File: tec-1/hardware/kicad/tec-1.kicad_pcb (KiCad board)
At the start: 2 copper layers, 160 x 160 mm, 150 parts, among them J1 USB_C_Receptacle_USB2.0, J2 Conn_01x02, J3 LCD, Q1 2N3904, Q10 AO3400A, Q11 AO3400A, Q12 AO3400A, Q13 AO3400A, Q14 AO3400A, Q15 AO3400A, Q16 AO3400A, Q17 AO3400A, Q18 AO3400A, Q19 AO3400A, Q2 AO3400A, Q20 AO3400A, Q21 AO3400A, Q22 AO3400A, Q23 AO3400A, Q3 AO3400A, Q4 AO3400A, Q5 AO3400A, Q6 AO3400A, Q7 AO3400A, Q8 AO3400A, Q9 AO3400A, SW1 SW_DIP_x04, SW10 SW_0, SW11 SW_7, SW12 SW_6, SW13 SW_5, SW14 SW_4, SW15 SW_B, SW16 SW_A, SW17 SW_9, SW18 SW_8, SW19 SW_F, SW2 SW_SPST, SW20 SW_E, SW21 SW_D, SW22 SW_C, SW3 SW_AD, SW4 SW_GO, SW5 SW_MINUS, SW6 SW_PLUS, SW7 SW_3, SW8 SW_2, SW9 SW_1, U1 IO, U10 74HCT574, U11 74HCT574, U12 LED_SEGMENT_CC_x2, U13 LED_SEGMENT_CC_x4, U14 74HCT574, U15 74HCT574, U16 74HCT574, U2 MEMORY, U3 Z80CPU, U5 SRM2264, U6 SRM2264, U7 FT232RL, U8 MM74C923, U9 KEYDB

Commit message: tec-1/hardware/kicad: progress checkin - add clock & 207 unrouted
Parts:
- added C20: 0.1uF/10V, tec-1:C_0805_2012Metric, F.Cu at (76.3, 82.8)
- added C21: 0.1uF/10V, tec-1:C_0805_2012Metric, B.Cu at (76.5, 99.5)
- added C8: 100uF/10V, tec-1:CP_EIA-7343-31_Kemet-D, F.Cu at (23.0, 147.5)
- added J4: ADDR, tec-1:PinHeader_1x17_P2.54mm_Vertical, F.Cu at (151.5, 68.0)
- added J5: DATA, tec-1:PinHeader_1x09_P2.54mm_Vertical, F.Cu at (160.8, 68.0)
- added R42: 10k, tec-1:R_0805_2012Metric, B.Cu at (79.5, 99.2)
- added R43: DNP, tec-1:R_0805_2012Metric, B.Cu at (84.2, 98.2)
- added R44: 10k, tec-1:R_0805_2012Metric, B.Cu at (52.0, 69.2)
- added R45: 10k, tec-1:R_0805_2012Metric, B.Cu at (52.0, 71.8)
- added R46: 10k, tec-1:R_0805_2012Metric, B.Cu at (52.0, 74.2)
- added R47: 10k, tec-1:R_0805_2012Metric, B.Cu at (52.0, 76.8)
- added SW23: SW_SPST, tec-1:SW_12x12_SMD, F.Cu at (129.5, 81.0)
- added SW24: SW_DIP_x04, tec-1:DIP-8_W7.62mm_LongPads, F.Cu at (55.8, 76.8)
- added TP26: TestPoint, tec-1:TestPoint_Pad_D2.0mm, B.Cu at (55.3, 139.5)
- added TP27: TestPoint, tec-1:TestPoint_Pad_D2.0mm, B.Cu at (51.5, 65.8)
- added TP28: TestPoint, tec-1:TestPoint_Pad_D2.0mm, B.Cu at (54.8, 65.8)
- added TP29: TestPoint, tec-1:TestPoint_Pad_D2.0mm, B.Cu at (48.3, 65.8)
- added TP30: TestPoint, tec-1:TestPoint_Pad_D2.0mm, B.Cu at (91.8, 85.2)
- added TP31: TestPoint, tec-1:TestPoint_Pad_D2.0mm, B.Cu at (91.9, 88.6)
- added U17: MISC, tec-1:PLCC-28_SMD-Socket, B.Cu at (72.2, 74.2)
- added U4: SST39SF040, tec-1:PLCC-32_SMD-Socket_9x7, F.Cu at (67.5, 56.2)
- added X1: 24MHz, tec-1:Oscillator_DIP-14_LargePads, F.Cu at (84.2, 103.0)
- C11, C12, C13, C14, C15, C16, C2, C3, C4, C5, C6, Q10, Q11, Q12, Q13, Q14, Q15, Q16, Q17, Q18, Q19, Q2, Q20, Q21, Q22, Q23, Q3, Q4, Q5, Q6, Q7, Q8, Q9, R10, R11, R12, R15, R16, R17, R18, R19, R2, R20, R21, R22, R23, R24, R25, R26, R27, R28, R29, R3, R30, R31, R32, R33, R34, R35, R36, R37, R38, R39, R4, R40, R41, R5, R6, R7, R8, R9, TP2, TP25, U1, U10, U11, U14, U15, U16, U2, U9: moved to B.Cu
- J2: footprint tec-1:PinHeader_1x02_P2.54mm_Vertical -> tec-1:JST_PH_S2B-PH-SM4-TB_1x02-1MP_P2.00mm_Horizontal; moved to B.Cu
- Q1: value 2N3904 -> BC847; footprint tec-1:TO-92_Inline -> tec-1:SOT-23; moved to B.Cu
- U8: footprint tec-1:DIP-18_W7.62mm_LongPads -> tec-1:DIP-20_W7.62mm_LongPads
- moved C6 375.0 mm to (139.5, 35.5), turned to 180 degrees
- moved R11 353.9 mm to (139.5, 41.0)
- moved C5 341.8 mm to (120.5, 35.5), turned to 180 degrees
- moved R10 341.0 mm to (120.5, 41.0)
- moved U8 331.4 mm to (85.0, 151.5), turned to 180 degrees
- moved C3 319.0 mm to (92.5, 58.5)
- moved U3 318.0 mm to (89.0, 33.0)
- moved U5 317.7 mm to (108.5, 35.7)
- moved U6 317.7 mm to (127.8, 35.7)
- moved R3 307.3 mm to (108.2, 71.8)
- moved R4 303.6 mm to (100.2, 71.2), turned to 180 degrees
- moved C11 300.3 mm to (81.0, 151.5)
- moved R2 296.8 mm to (108.2, 74.2)
- moved C12 296.4 mm to (81.5, 136.0), turned to 180 degrees
- moved C4 295.6 mm to (68.0, 46.0), turned to 180 degrees
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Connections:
- net Net-(C7-Pad2) renamed /keybd/SHIELD
- net Net-(J1-PadA5) renamed /keybd/CC1
- net Net-(J1-PadB5) renamed /keybd/CC2
- net Net-(Q2-Pad1) renamed /displays/COLEN_5
- net Net-(Q2-Pad3) renamed /displays/COL_5R
- net Net-(Q3-Pad1) renamed /displays/COLEN_4
- net Net-(Q3-Pad3) renamed /displays/COL_4R
- net Net-(Q4-Pad1) renamed /displays/COLEN_3
- net Net-(Q4-Pad3) renamed /displays/COL_3R
- net Net-(Q5-Pad1) renamed /displays/COLEN_2
- net Net-(Q5-Pad3) renamed /displays/COL_2R
- net Net-(Q6-Pad1) renamed /displays/COLEN_1
- net Net-(Q6-Pad3) renamed /displays/COL_1R
- net Net-(Q7-Pad1) renamed /displays/COLEN_0
- net Net-(Q7-Pad3) renamed /displays/COL0_R
- net Net-(R1-Pad1) renamed /~INT
- net Net-(R18-Pad1) renamed /displays/SPEN
- net Net-(R2-Pad1) renamed /~WAIT
- net Net-(R4-Pad1) renamed /~BUSRQ
- net Net-(U3-Pad27) renamed /~M1
- Q1 pad 1: GND -> Net-(Q1-Pad1)
- Q1 pad 2: Net-(Q1-Pad2) -> GND
- Q13 pad 1: GND -> Net-(Q13-Pad1)
- Q8 pad 1: Net-(Q15-Pad1) -> Net-(Q8-Pad1)
- R18 pad 2: Net-(Q1-Pad2) -> Net-(Q1-Pad1)
- U1 pad 2: Net-(U1-Pad18) -> Net-(TP26-Pad1)
- U1 pad 25: /D6 -> Net-(U1-Pad25)
- U1 pad 27: /KEYBD_CS -> Net-(U1-Pad27)
- U10 pad 12: /displays/SEG_D -> /displays/SEG_A
- U10 pad 13: /displays/SEG_E -> /displays/SEG_F
- U10 pad 14: /displays/SEG_C -> /displays/SEG_G
- U10 pad 15: /displays/SEG_DP -> /displays/SEG_B
- U10 pad 16: /displays/SEG_B -> /displays/SEG_DP
- U10 pad 17: /displays/SEG_G -> /displays/SEG_C
- U10 pad 18: /displays/SEG_F -> /displays/SEG_E
- U10 pad 19: /displays/SEG_A -> /displays/SEG_D
- U10 pad 2: /D0 -> /D7
- U10 pad 3: /D1 -> /D6
- U10 pad 4: /D2 -> /D5
- U10 pad 5: /D3 -> /D4
- U10 pad 6: /D4 -> /D3
- U10 pad 7: /D5 -> /D2
- U10 pad 8: /D6 -> /D1
- U10 pad 9: /D7 -> /D0
- U14 pad 13: Net-(Q10-Pad1) -> Net-(Q13-Pad1)
- U14 pad 14: Net-(Q12-Pad1) -> Net-(Q11-Pad1)
- U14 pad 15: Net-(Q14-Pad1) -> Net-(Q9-Pad1)
- U14 pad 16: Net-(Q9-Pad1) -> Net-(Q14-Pad1)
- U14 pad 17: Net-(Q11-Pad1) -> Net-(Q12-Pad1)
- U14 pad 18: GND -> Net-(Q10-Pad1)
- U14 pad 19: Net-(Q15-Pad1) -> Net-(Q8-Pad1)
- U14 pad 2: /D0 -> /D7
- U14 pad 3: /D1 -> /D6
- U14 pad 4: /D2 -> /D5
- U14 pad 5: /D3 -> /D4
- U14 pad 6: /D4 -> /D3
- U14 pad 7: /D5 -> /D2
- U14 pad 8: /D6 -> /D1
- U14 pad 9: /D7 -> /D0
- U3 pad 6: Net-(U3-Pad6) -> /~CLK
- U7 pad 2: /keybd/FTDI_D3 -> /keybd/FTDI_D4
- U9 pad 10: /keybd/FTDI_D3 -> /keybd/FTDI_D4
- U9 pad 15: /keybd/~SHIFT_KEY -> Net-(U9-Pad15)
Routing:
- net +5V: track 0.00 -> 888.7 mm, vias 0 -> 22
- net /D4: track 0.00 -> 403.9 mm, vias 0 -> 7
- net /D3: track 0.00 -> 389.7 mm, vias 0 -> 4
- net /D2: track 0.00 -> 374.6 mm, vias 0 -> 5
- net /D0: track 0.00 -> 367.9 mm, vias 0 -> 2
- net /D5: track 0.00 -> 363.9 mm, vias 0 -> 7
- net /D1: track 0.00 -> 363.2 mm, vias 0 -> 3
- net /A7: track 0.00 -> 344.4 mm, vias 0 -> 8
- net /D6: track 0.00 -> 344.2 mm, vias 0 -> 7
- net /D7: track 0.00 -> 338.5 mm, vias 0 -> 5
- net /~WR: track 0.00 -> 289.2 mm, vias 0 -> 7
- net /A3: track 0.00 -> 276.7 mm, vias 0 -> 5
- net /A2: track 0.00 -> 263.4 mm, vias 0 -> 5
- net /A1: track 0.00 -> 249.6 mm, vias 0 -> 5
- net /A0: track 0.00 -> 239.4 mm, vias 0 -> 3
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- added copper zone on B.Cu, net /keybd/SHIELD

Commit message: tec-1/hardware/kicad: routing complete, all DRC errors checked as ok
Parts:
- removed TP10, TP11, TP12, TP14, TP15, TP17, TP19, TP20, TP21, TP23, TP26, TP4, TP6, TP7, TP8, TP9: TestPoint, tec-1:TestPoint_Pad_D2.0mm
- added C22: 0.1uF/10V, tec-1:C_0805_2012Metric, F.Cu at (32.2, 166.2)
- added D3: LED, tec-1:LED_0805_2012Metric, F.Cu at (37.2, 153.3)
- added J6: Conn_01x02, tec-1:PinHeader_1x02_P2.54mm_Vertical, F.Cu at (172.8, 142.5)
- added R48: 1k, tec-1:R_0805_2012Metric, F.Cu at (37.2, 149.8)
- added RV1: 20k, tec-1:Potentiometer_Bourns_TC33X_Vertical, F.Cu at (80.4, 166.2)
- TP1, TP13, TP16, TP18, TP22, TP24, TP3, TP5: moved to B.Cu
- moved TP24 252.2 mm to (39.0, 167.4)
- moved TP22 248.0 mm to (37.6, 162.1)
- moved TP13 216.4 mm to (69.0, 50.1)
- moved TP5 149.0 mm to (78.6, 30.5)
- moved TP3 138.7 mm to (78.6, 36.6)
- moved TP18 111.7 mm to (56.3, 40.6)
- moved TP16 52.3 mm to (40.8, 162.1)
- moved TP1 33.8 mm to (25.5, 145.5)
- moved R9 1.34 mm to (70.2, 56.7), turned to 270 degrees
- moved R14 1.06 mm to (30.2, 166.2), turned to 90 degrees
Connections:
- R16 pad 1: Net-(J2-Pad2) -> Net-(Q1-Pad3)
- R16 pad 2: Net-(Q1-Pad3) -> Net-(J6-Pad1)
- U1 pad 18: Net-(U1-Pad18) -> /KEYBD_CS
- U12 pad 1: /displays/SEG_D -> /displays/SEG_C
- U12 pad 10: /displays/COL_0 -> /displays/SEG_A
- U12 pad 4: /displays/SEG_C -> /displays/SEG_D
- U12 pad 5: /displays/COL_1 -> /displays/SEG_G
- U12 pad 6: /displays/SEG_B -> /displays/SEG_F
- U12 pad 7: /displays/SEG_A -> /displays/COL_0
- U12 pad 8: /displays/SEG_F -> /displays/COL_1
- U12 pad 9: /displays/SEG_G -> /displays/SEG_B
- U2 pad 2: Net-(TP12-Pad1) -> /~M1
- U2 pad 26: Net-(TP19-Pad1) -> /~INT
- U9 pad 17: (no net) -> Net-(U9-Pad17)
- U9 pad 2: Net-(U9-Pad2) -> Net-(U7-Pad23)
- U9 pad 27: Net-(U9-Pad2) -> Net-(U9-Pad27)
- U9 pad 4: Net-(U7-Pad23) -> /keybd/~SHIFT_KEY
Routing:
- net +5V: track 888.7 -> 1078.1 mm, vias 22 -> 32
- net /~M1: track 0.00 -> 102.6 mm, vias 0 -> 3
- net /displays/SEG_F: track 0.00 -> 95.0 mm, vias 0 -> 2
- net /displays/SEG_D: track 0.00 -> 93.5 mm, vias 0 -> 2
- net /displays/SEG_E: track 0.00 -> 90.7 mm, vias 0 -> 2
- net /displays/SEG_A: track 0.00 -> 85.2 mm, vias 0 -> 1
- net /displays/SPEN: track 0.00 -> 84.7 mm, vias 0 -> 2
- net /D7: track 338.5 -> 422.2 mm, vias 5 -> 8
- net /displays/SEG_G: track 0.00 -> 82.9 mm, vias 0 -> 1
- net /displays/SEG_B: track 0.00 -> 80.6 mm, vias 0 -> 1
- net /D6: track 344.2 -> 424.2 mm, vias 7 -> 10
- net /displays/SEG_DP: track 0.00 -> 79.7 mm, vias 0 -> 2
- net /D5: track 363.9 -> 441.2 mm, vias 7 -> 11
- net /~INT: track 4.63 -> 75.7 mm, vias 0 -> 3
- net /D0: track 367.9 -> 436.6 mm, vias 2 -> 4
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- added copper zone on B.Cu, net GND
- added copper zone on F.Cu, net GND

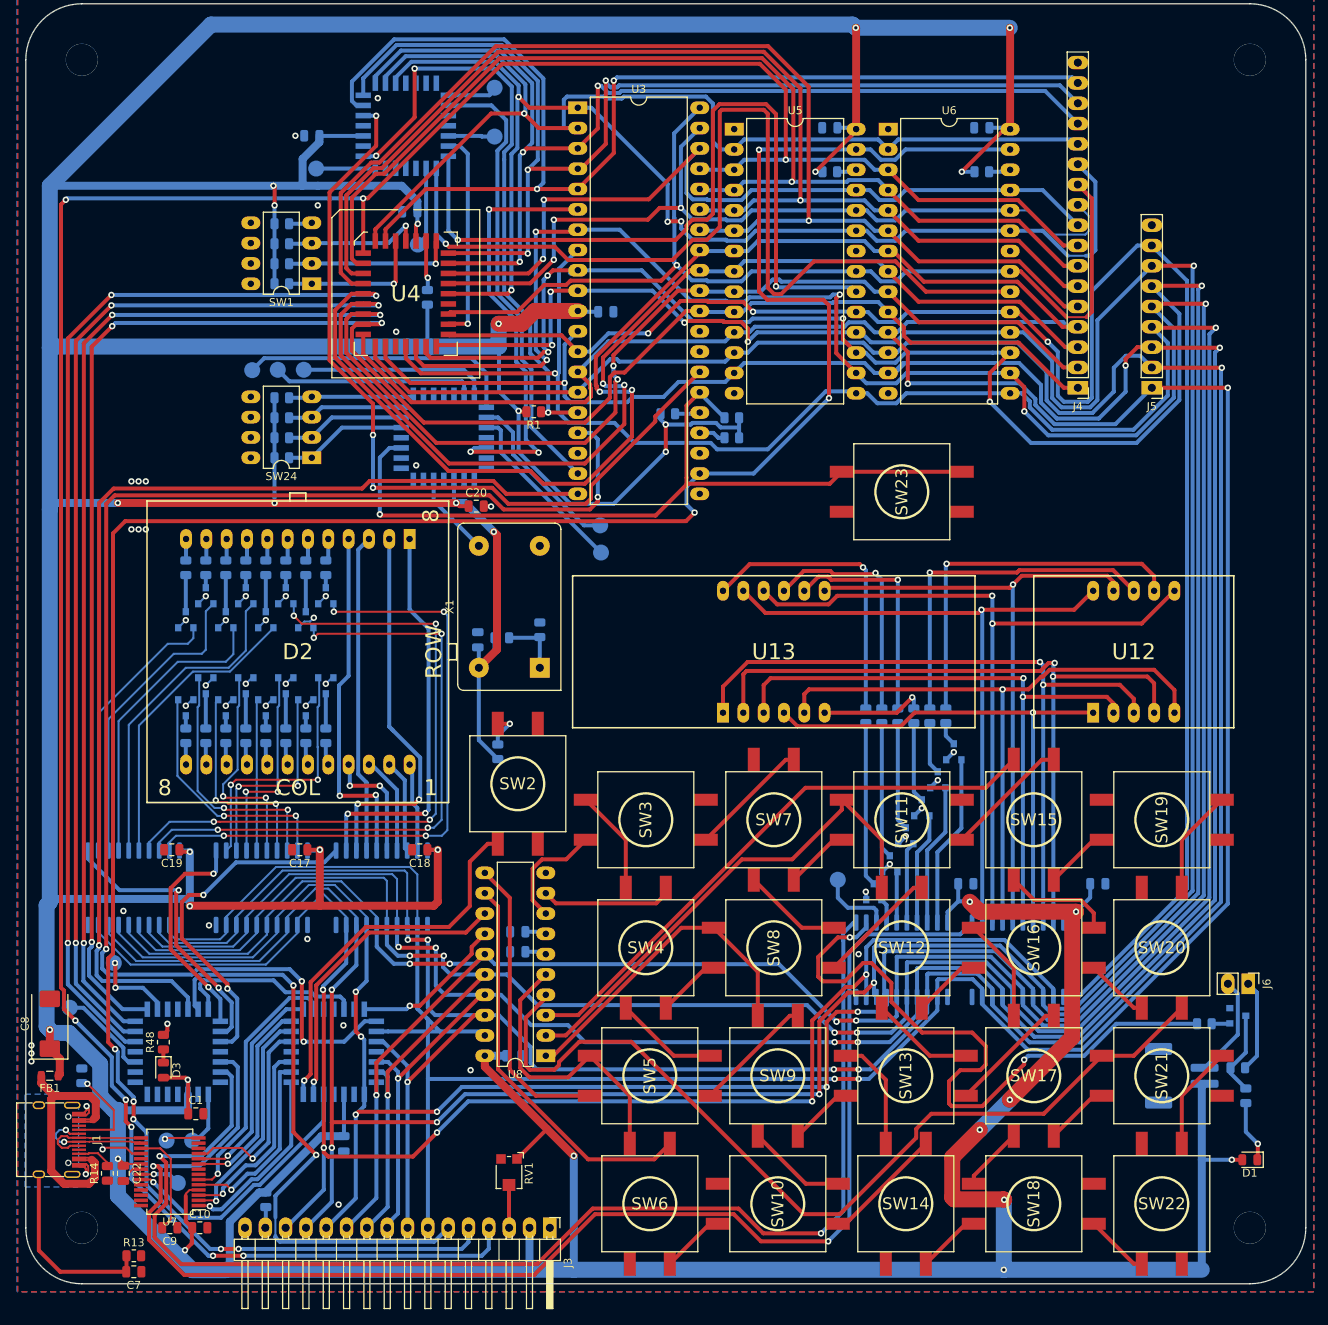
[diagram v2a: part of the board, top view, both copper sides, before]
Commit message: tec-1/hardware/kicad: added ctrl header, fixed keypad alignment
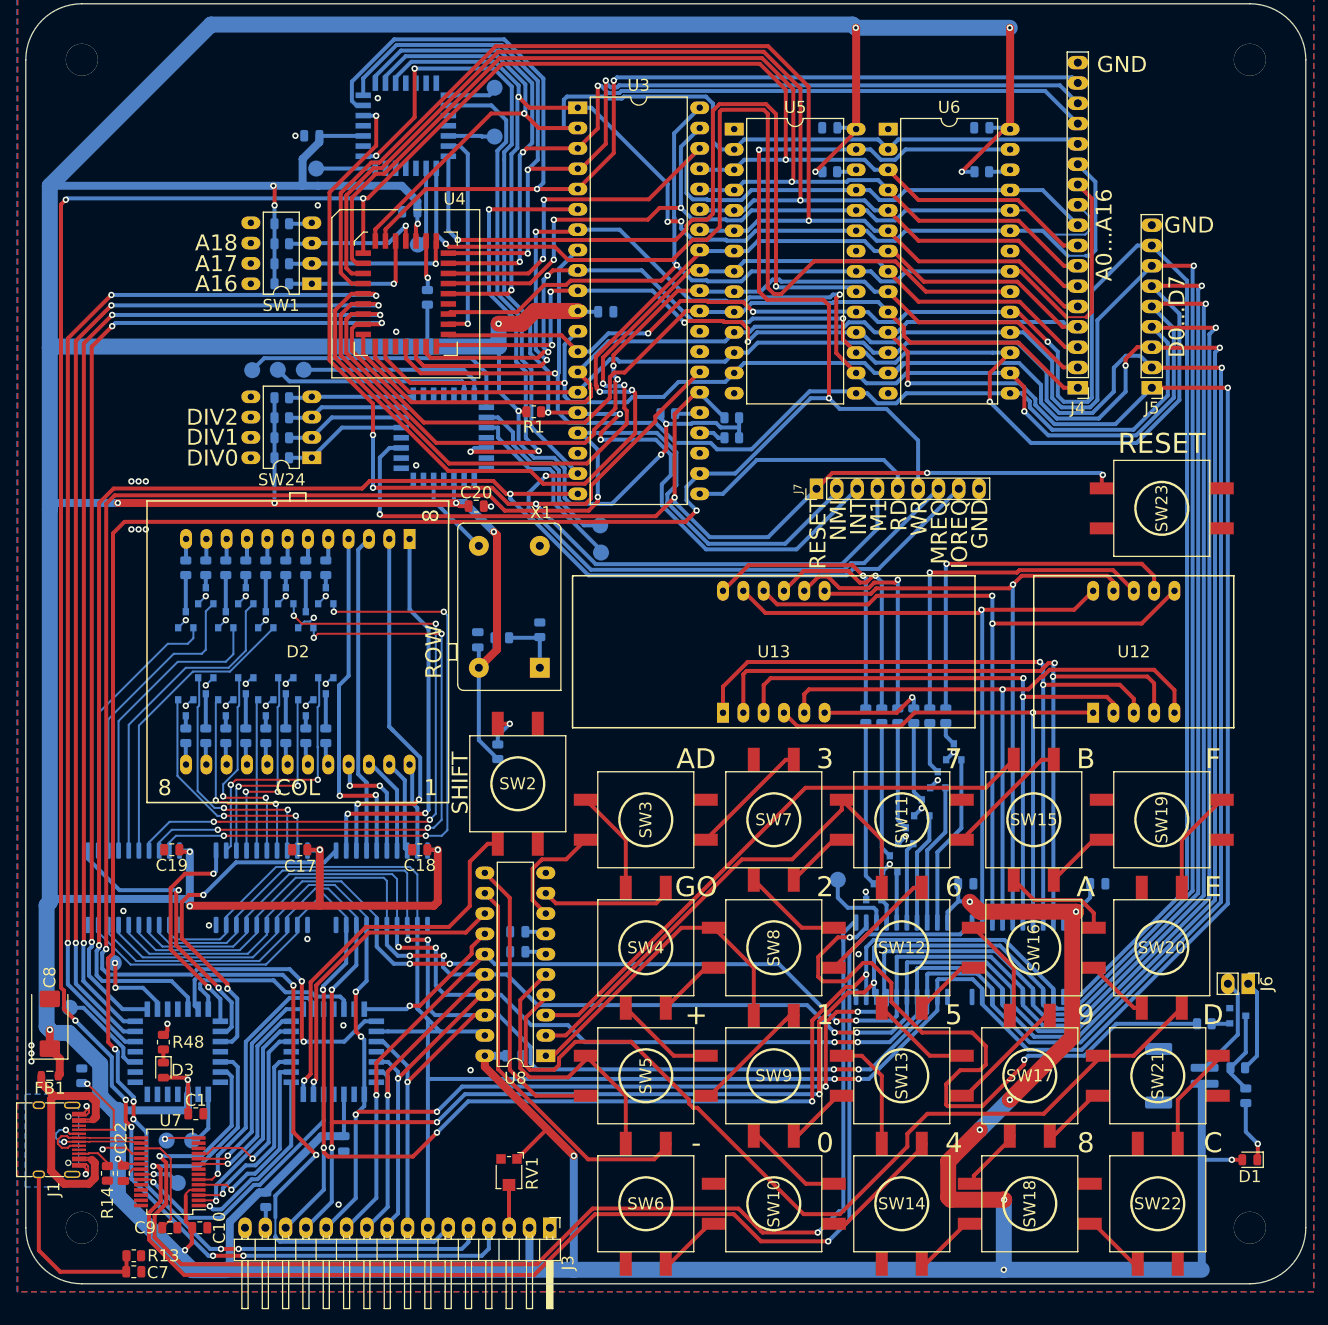
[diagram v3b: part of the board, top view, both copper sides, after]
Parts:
- added J7: CTRL, tec-1:PinHeader_1x09_P2.54mm_Vertical, F.Cu at (118.8, 80.6)
- moved SW23 32.6 mm to (162.0, 83.1)
- moved SW10 0.50 mm to (113.5, 170.0)
- moved SW13 0.50 mm to (129.5, 154.0)
- moved SW14 0.50 mm to (129.5, 170.0)
- moved SW17 0.50 mm to (145.5, 154.0)
- moved SW18 0.50 mm to (145.5, 170.0)
- moved SW21 0.50 mm to (161.5, 154.0)
- moved SW22 0.50 mm to (161.5, 170.0)
- moved SW5 0.50 mm to (97.5, 154.0)
- moved SW6 0.50 mm to (97.5, 170.0)
- moved SW9 0.50 mm to (113.5, 154.0)
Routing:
- net /~MREQ: track 56.8 -> 124.5 mm, vias 0 -> 1
- net /~IOREQ: track 134.8 -> 200.0 mm, vias 1 -> 2
- net /~INT: track 75.7 -> 131.4 mm, vias 3 -> 5
- net /~M1: track 102.6 -> 155.3 mm, vias 3 -> 4
- net /~NMI: track 175.9 -> 221.8 mm
- net /~RD: track 0.00 -> 29.1 mm
- net /~RESET: track 102.1 -> 128.4 mm, vias 1 -> 4
- net /~WR: track 300.7 -> 320.2 mm
- net +5V: track 1078.1 -> 1080.2 mm
- net /keybd/X1: track 89.0 -> 91.0 mm
- net Net-(TP31-Pad1): track 22.4 -> 23.9 mm
- net Net-(TP30-Pad1): track 21.4 -> 22.9 mm
- net /keybd/Y4: track 140.2 -> 141.3 mm
- net /keybd/X2: track 83.7 -> 84.7 mm
- net /displays/COL_3: track 28.7 -> 29.6 mm
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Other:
- board text added: "+"
- board text added: "-"
- board text added: "0"
- board text added: "1"
- board text added: "2"
- board text added: "3"
- board text added: "4"
- board text added: "5"
- board text added: "6"
- board text added: "7"
- board text added: "8"
- board text added: "9"
- board text added: "A"
- board text added: "A0...A16"
- board text added: "A16"
- board text added: "A17"
- board text added: "A18"
- board text added: "AD"
- board text added: "B"
- board text added: "C"
- board text added: "D"
- board text added: "D0...D7"
- board text added: "DIV0"
- board text added: "DIV1"
- board text added: "DIV2"
- board text added: "E"
- board text added: "F"
- board text added: "GND"
- board text added: "GO"
- board text added: "INT"
- board text added: "IOREQ"
- board text added: "M1"
- board text added: "MREQ"
- board text added: "NMI"
- board text added: "RD"
- board text added: "RESET"
- board text added: "SHIFT"
- board text added: "WR"

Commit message: tec-1/hardware/kicad: apr2021 release
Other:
- board text added: "@TomKeddie Apr2021"
- board text added: "Z80"
